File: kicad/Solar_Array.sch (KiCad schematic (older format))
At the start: 26 parts

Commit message: Changed XSHUT to pin header.
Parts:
- removed C?: C, symbol C
- removed C?: .1u, symbol C
- removed D?: ZENER, symbol ZENER
- removed R?: R, symbol R
- removed R?: 10k, symbol R
- removed SW?: SW_PUSH, symbol SW_PUSH
- added P?: X_SHUT, symbol CONN_01X01
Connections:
- wire segments 74 -> 66
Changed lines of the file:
@@
 	1    0    0    -1
-$EndComp
-$Comp
-L R R?
-U 1 1 56A86498
-P 16050 6750
-F 0 "R?" V 16130 6750 50  0000 C CNN
-F 1 "R" V 16050 6750 50  0000 C CNN
-F 2 "" V 15980 6750 30  0000 C CNN
-F 3 "" H 16050 6750 30  0000 C CNN
-	1    16050 6750
-	1    0    0    -1
-$EndComp
-$Comp
-L C C?
-U 1 1 56A86782
-P 16050 7300
-F 0 "C?" H 16075 7400 50  0000 L CNN
-F 1 "C" H 16075 7200 50  0000 L CNN
-F 2 "" H 16088 7150 30  0000 C CNN
-F 3 "" H 16050 7300 60  0000 C CNN
-	1    16050 7300
-	1    0    0    -1
-$EndComp
-$Comp
-L ZENER D?
-U 1 1 56A86C34
-P 16050 8000
-F 0 "D?" H 16050 8100 50  0000 C CNN
-F 1 "ZENER" H 16050 7900 50  0000 C CNN
-F 2 "" H 16050 8000 60  0000 C CNN
-F 3 "" H 16050 8000 60  0000 C CNN
-	1    16050 8000
-	0    1    1    0
 $EndComp
 Text Notes 1200 9750 0    60   ~ 0
@@
 	6050 1300 9000 1300
 Wire Wire Line
-	16050 5850 16050 6600
-Connection ~ 16050 5850
-Wire Wire Line
-	16050 6900 16050 7150
-Wire Wire Line
-	16050 7450 16050 7800
-Wire Wire Line
-	16050 8200 16050 8900
-Connection ~ 16050 8900
-Wire Wire Line
 	1400 2850 1550 2850
 Wire Wire Line
@@
 Connection ~ 3900 2250
 Wire Wire Line
-	3600 1700 5150 1700
-Wire Wire Line
 	3900 1350 3900 1800
 Connection ~ 4900 1700
@@
 	-1   0    0    1
 $EndComp
-$Comp
-L SW_PUSH SW?
-U 1 1 56A9E4AC
-P 3100 3650
-F 0 "SW?" H 3250 3760 50  0000 C CNN
-F 1 "SW_PUSH" H 3100 3570 50  0000 C CNN
-F 2 "" H 3100 3650 60  0000 C CNN
-F 3 "" H 3100 3650 60  0000 C CNN
-	1    3100 3650
-	0    1    1    0
-$EndComp
-Wire Wire Line
-	3100 3950 3100 4050
-$Comp
-L GND #PWR?
-U 1 1 56A9E5E0
-P 3100 4400
-F 0 "#PWR?" H 3100 4150 50  0001 C CNN
-F 1 "GND" H 3100 4250 50  0000 C CNN
-F 2 "" H 3100 4400 60  0000 C CNN
-F 3 "" H 3100 4400 60  0000 C CNN
-	1    3100 4400
-	1    0    0    -1
-$EndComp
-Wire Wire Line
-	3100 1700 3100 3350
 Wire Wire Line
 	3100 3300 3250 3300
-Wire Wire Line
-	3100 1700 3300 1700
 Connection ~ 3100 3300
-$Comp
-L C C?
-U 1 1 56A9E786
-P 3450 1700
-F 0 "C?" H 3475 1800 50  0000 L CNN
-F 1 ".1u" H 3475 1600 50  0000 L CNN
-F 2 "" H 3488 1550 30  0000 C CNN
-F 3 "" H 3450 1700 60  0000 C CNN
-	1    3450 1700
-	0    1    1    0
-$EndComp
-$Comp
-L R R?
-U 1 1 56A9EACC
-P 3100 4200
-F 0 "R?" V 3180 4200 50  0000 C CNN
-F 1 "10k" V 3100 4200 50  0000 C CNN
-F 2 "" V 3030 4200 30  0000 C CNN
-F 3 "" H 3100 4200 30  0000 C CNN
-	1    3100 4200
-	1    0    0    -1
-$EndComp
-Wire Wire Line
-	3100 4350 3100 4400
+Wire Wire Line
+	3900 1700 5150 1700
+$Comp
+L CONN_01X01 P?
+U 1 1 56AA3494
+P 2900 3300
+F 0 "P?" H 2900 3400 50  0000 C CNN
+F 1 "X_SHUT" H 2900 3200 50  0000 C CNN
+F 2 "" H 2900 3300 60  0000 C CNN
+F 3 "" H 2900 3300 60  0000 C CNN
+	1    2900 3300
+	-1   0    0    1
+$EndComp
 $EndSCHEMATC

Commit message: Removed extraneous circuitry, added more component values, swapped 1x2 conn with 1x3 conn.
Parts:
- removed C?: .1u, symbol C
- removed P?: V_BATT, symbol CONN_01X02
- added D?: D_Schottky, symbol D_Schottky
- added P?: V_BATT, symbol CONN_01X03
- R?: value R -> .007
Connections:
- net labels removed: +5V
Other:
- note added: "VCC_IN"
- moved on the sheet: P?
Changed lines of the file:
@@
-	1    0    0    -1
-$EndComp
-$Comp
-L +5V #PWR?
-U 1 1 56A796A0
-P 7300 1800
-F 0 "#PWR?" H 7300 1650 50  0001 C CNN
-F 1 "+5V" H 7300 1940 50  0000 C CNN
-F 2 "" H 7300 1800 60  0000 C CNN
-F 3 "" H 7300 1800 60  0000 C CNN
-	1    7300 1800
 	1    0    0    -1
 $EndComp
@@
 L GND #PWR?
 U 1 1 56A96BD7
-P 1550 2950
-F 0 "#PWR?" H 1550 2700 50  0001 C CNN
-F 1 "GND" H 1550 2800 50  0000 C CNN
-F 2 "" H 1550 2950 60  0000 C CNN
-F 3 "" H 1550 2950 60  0000 C CNN
-	1    1550 2950
+P 1250 3100
+F 0 "#PWR?" H 1250 2850 50  0001 C CNN
+F 1 "GND" H 1250 2950 50  0000 C CNN
+F 2 "" H 1250 3100 60  0000 C CNN
+F 3 "" H 1250 3100 60  0000 C CNN
+	1    1250 3100
 	1    0    0    -1
 $EndComp
@@
 P 4900 2250
 F 0 "R?" V 4980 2250 50  0000 C CNN
-F 1 "R" V 4900 2250 50  0000 C CNN
+F 1 ".007" V 4900 2250 50  0000 C CNN
 F 2 "" V 4830 2250 30  0000 C CNN
 F 3 "" H 4900 2250 30  0000 C CNN
@@
 	7000 3350 7000 3600
 Wire Wire Line
-	7300 1800 7300 2150
+	7300 1050 7300 2150
 Wire Wire Line
 	7600 2950 7850 2950
@@
 Wire Notes Line
 	6050 1300 9000 1300
-Wire Wire Line
-	1400 2850 1550 2850
-Wire Wire Line
-	1550 2850 1550 2950
-Wire Wire Line
-	1400 2750 2450 2750
 Wire Wire Line
 	2350 2750 2350 3050
@@
 Wire Wire Line
 	4700 2250 4550 2250
-$Comp
-L GND #PWR?
-U 1 1 56A9D3E6
-P 2500 2350
-F 0 "#PWR?" H 2500 2100 50  0001 C CNN
-F 1 "GND" H 2500 2200 50  0000 C CNN
-F 2 "" H 2500 2350 60  0000 C CNN
-F 3 "" H 2500 2350 60  0000 C CNN
-	1    2500 2350
-	1    0    0    -1
-$EndComp
-$Comp
-L C C?
-U 1 1 56A9D482
-P 2850 2250
-F 0 "C?" H 2875 2350 50  0000 L CNN
-F 1 ".1u" H 2875 2150 50  0000 L CNN
-F 2 "" H 2888 2100 30  0000 C CNN
-F 3 "" H 2850 2250 60  0000 C CNN
-	1    2850 2250
-	0    1    1    0
-$EndComp
-Wire Wire Line
-	2700 2250 2500 2250
-Wire Wire Line
-	2500 2250 2500 2350
-Wire Wire Line
-	3000 2250 4250 2250
 Connection ~ 3900 2250
 Wire Wire Line
@@
 Wire Wire Line
 	6000 1150 4000 1150
-$Comp
-L CONN_01X02 P?
-U 1 1 56A9DC7C
-P 9450 1000
-F 0 "P?" H 9450 1150 50  0000 C CNN
-F 1 "V_BATT" V 9550 1000 50  0000 C CNN
-F 2 "" H 9450 1000 60  0000 C CNN
-F 3 "" H 9450 1000 60  0000 C CNN
-	1    9450 1000
-	1    0    0    -1
-$EndComp
 Wire Wire Line
 	3900 950  9250 950
-Wire Wire Line
-	9250 1050 9150 1050
-Wire Wire Line
-	9150 1050 9150 1300
 $Comp
 L GND #PWR?
@@
 L CONN_01X02 P?
 U 1 1 56A9E16B
-P 1200 2800
-F 0 "P?" H 1200 2950 50  0000 C CNN
-F 1 "PV_CELL" V 1300 2800 50  0000 C CNN
-F 2 "" H 1200 2800 60  0000 C CNN
-F 3 "" H 1200 2800 60  0000 C CNN
-	1    1200 2800
+P 850 2800
+F 0 "P?" H 850 2950 50  0000 C CNN
+F 1 "PV_CELL" V 950 2800 50  0000 C CNN
+F 2 "" H 850 2800 60  0000 C CNN
+F 3 "" H 850 2800 60  0000 C CNN
+	1    850  2800
 	-1   0    0    1
 $EndComp
@@
 	-1   0    0    1
 $EndComp
+Wire Wire Line
+	3900 2250 4250 2250
+$Comp
+L CONN_01X03 P?
+U 1 1 56AA5ABE
+P 9450 1050
+F 0 "P?" H 9450 1250 50  0000 C CNN
+F 1 "V_BATT" H 9650 1150 50  0000 C CNN
+F 2 "" H 9450 1050 60  0000 C CNN
+F 3 "" H 9450 1050 60  0000 C CNN
+	1    9450 1050
+	1    0    0    -1
+$EndComp
+Wire Wire Line
+	9150 1150 9250 1150
+Wire Wire Line
+	9150 1150 9150 1300
+Wire Wire Line
+	7300 1050 9250 1050
+Text Notes 9550 1050 0    50   ~ 0
+VCC_IN
+$Comp
+L D_Schottky D?
+U 1 1 56AA70D2
+P 1500 2750
+F 0 "D?" H 1500 2850 50  0000 C CNN
+F 1 "D_Schottky" H 1500 2650 50  0000 C CNN
+F 2 "" H 1500 2750 60  0000 C CNN
+F 3 "" H 1500 2750 60  0000 C CNN
+	1    1500 2750
+	-1   0    0    1
+$EndComp
+Wire Wire Line
+	1050 2750 1350 2750
+Wire Wire Line
+	1050 2850 1250 2850
+Wire Wire Line
+	1250 2850 1250 3100
+Wire Wire Line
+	1650 2750 2450 2750
 $EndSCHEMATC

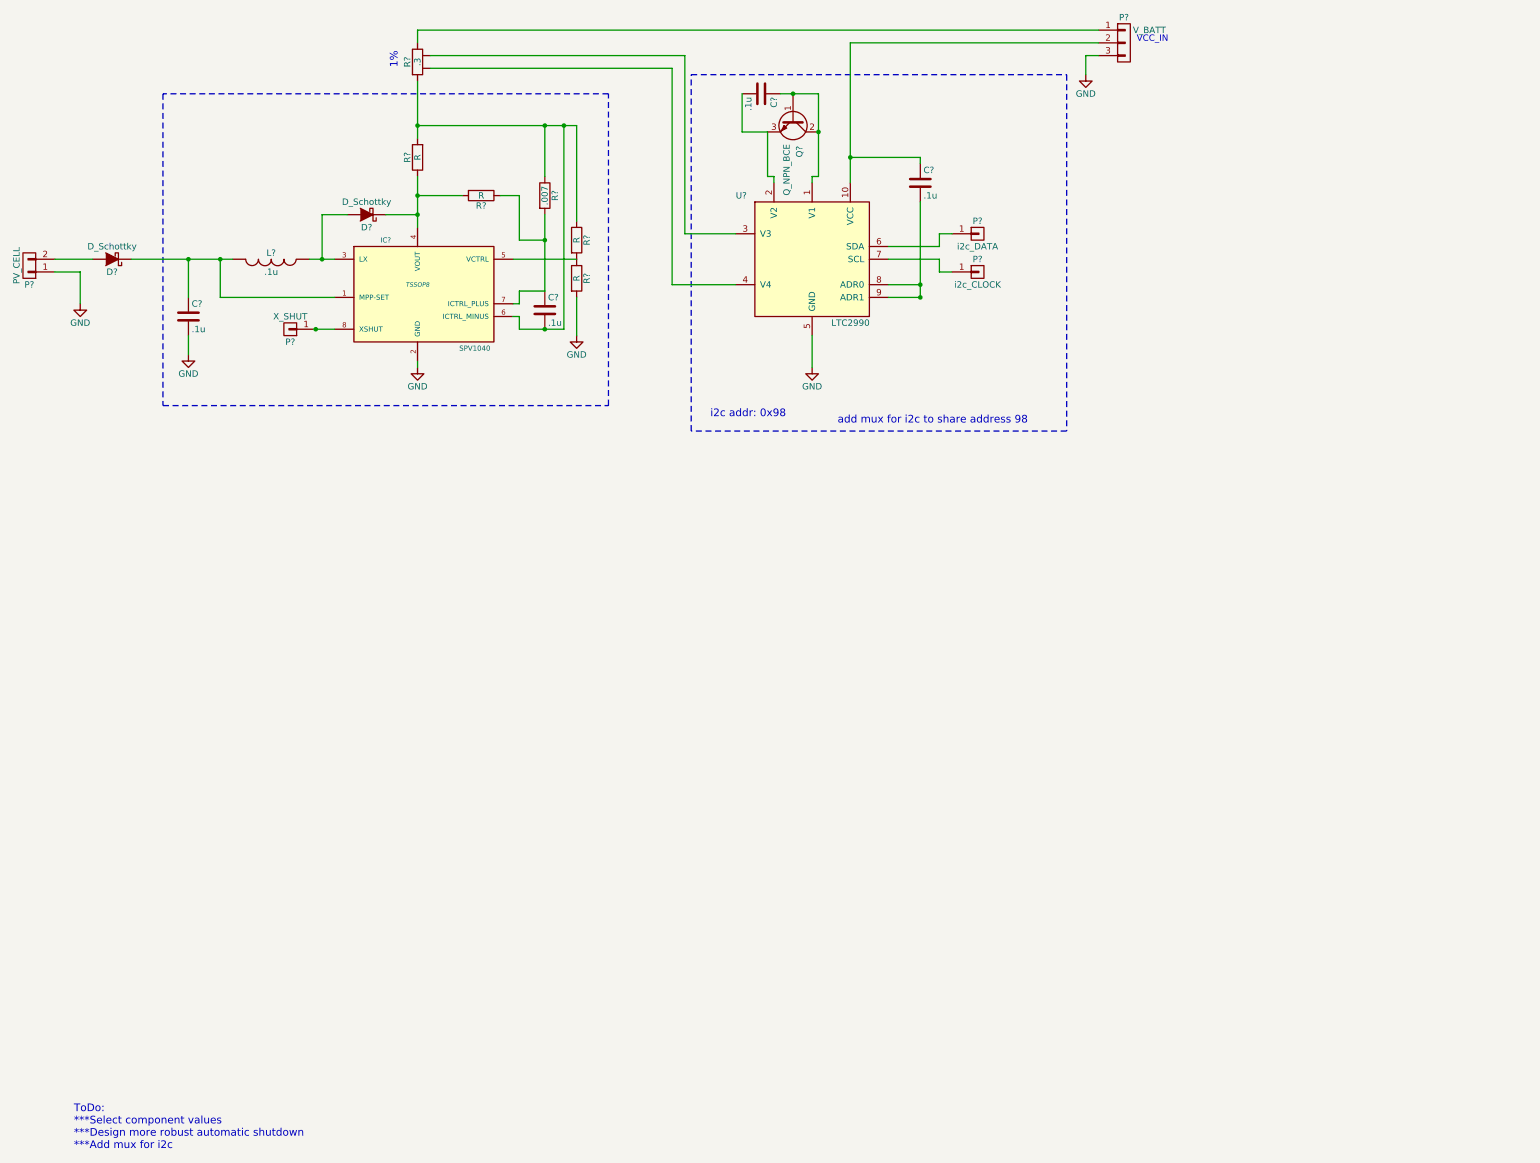
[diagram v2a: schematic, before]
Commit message: Changed Requirements, Notes, Outputs. Added Reference Switch.  Design Docs Updated.
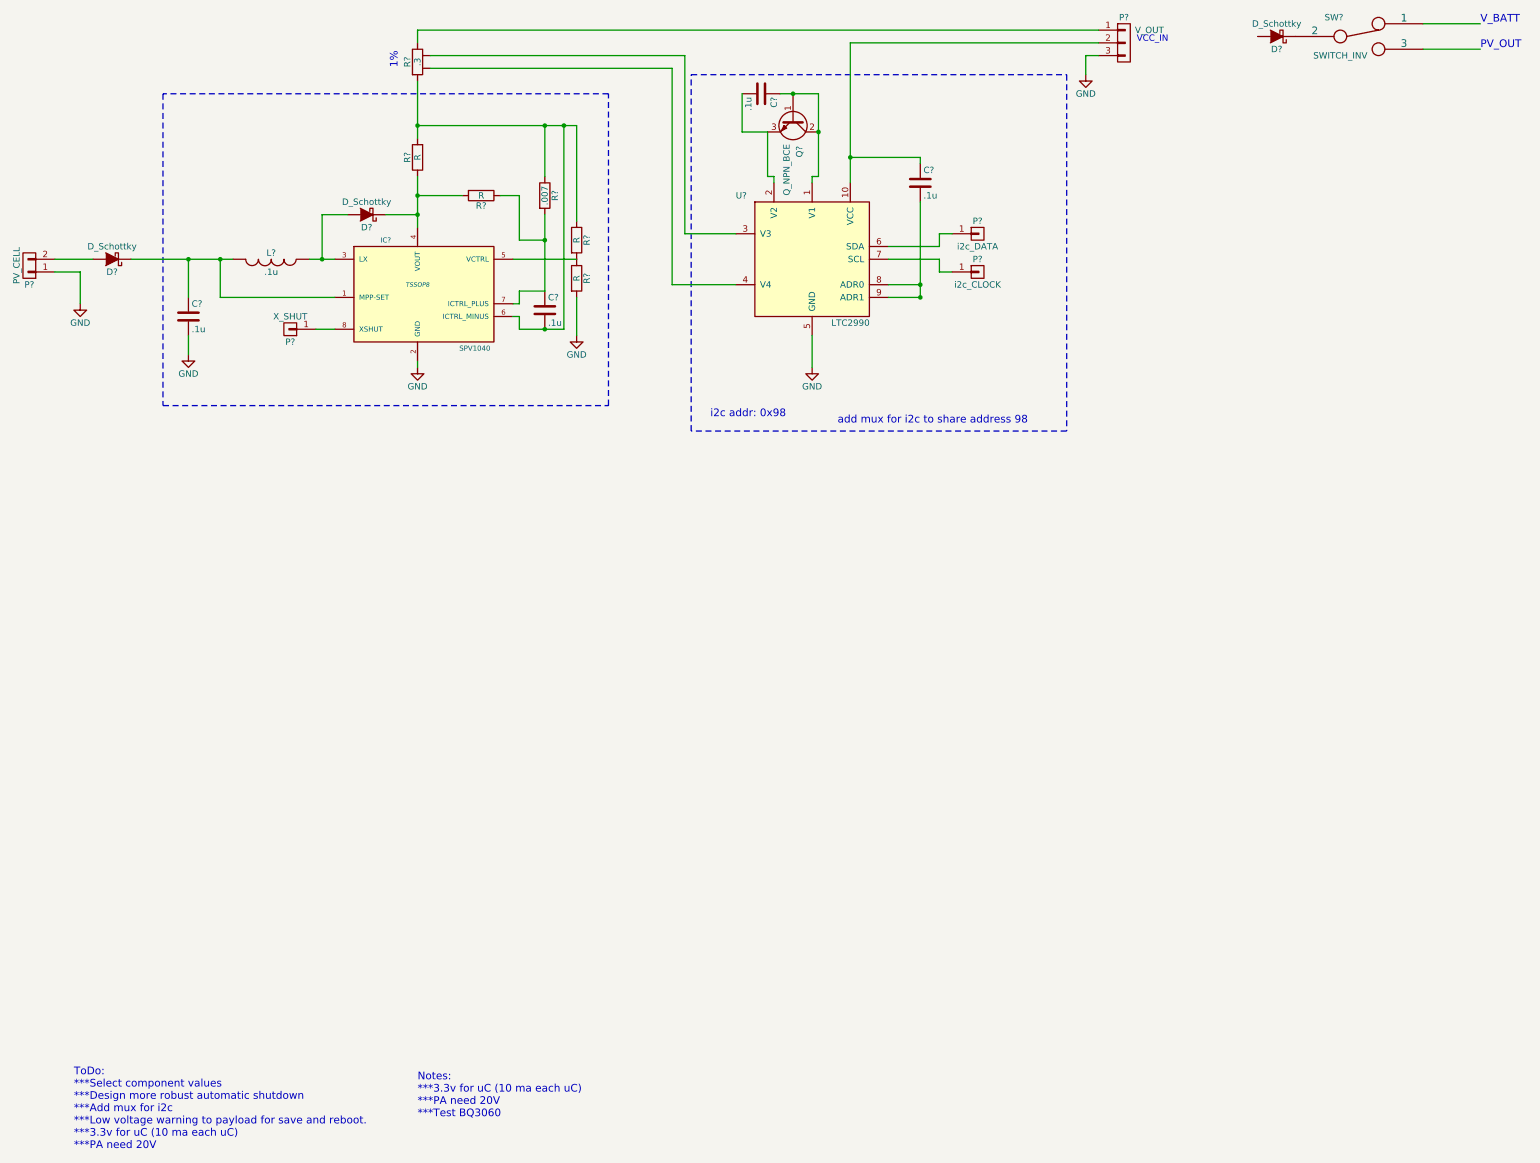
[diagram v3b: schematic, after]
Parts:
- added D?: D_Schottky, symbol D_Schottky
- added SW?: SWITCH_INV, symbol SWITCH_INV
- P?: value V_BATT -> V_OUT
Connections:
- new net: D?.1 (K), SW?.2
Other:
- note added: "Notes:\n***3.3v for uC (10 ma each uC)\n***PA need 20V\n***Test BQ3060"
- note added: "PV_OUT"
- note added: "ToDo:\n***Select component values\n***Design more robust automatic shutdown\n***Add mux for i2c\n***Low voltage warning to payload for save and reboot.\n***3.3v for uC (10 ma each uC)\n***PA need 20V"
- note added: "V_BATT"
- note removed: "ToDo:\n***Select component values\n***Design more robust automatic shutdown\n***Add mux for i2c\n"
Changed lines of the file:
@@
 $EndComp
 Text Notes 1200 9750 0    60   ~ 0
-ToDo:\n***Select component values\n***Design more robust automatic shutdown\n***Add mux for i2c\n
+ToDo:\n***Select component values\n***Design more robust automatic shutdown\n***Add mux for i2c\n***Low voltage warning to payload for save and reboot.\n***3.3v for uC (10 ma each uC)\n***PA need 20V
 Text Notes 3750 1250 1    60   ~ 0
 1%
@@
 	1    0    0    -1
 $EndComp
-Wire Wire Line
-	7000 3350 7000 3600
-Wire Wire Line
-	7300 1050 7300 2150
-Wire Wire Line
-	7600 2950 7850 2950
-Wire Wire Line
-	7850 3050 7600 3050
-Connection ~ 7850 3050
-Connection ~ 7850 2950
-Wire Wire Line
-	7850 2000 7850 1950
-Wire Wire Line
-	7850 1950 7300 1950
-Connection ~ 7300 1950
-Wire Notes Line
-	9000 1300 9000 4100
-Wire Notes Line
-	9000 4100 6050 4100
-Wire Notes Line
-	6050 4100 6050 1300
-Wire Wire Line
-	7850 2300 7850 3050
-Wire Wire Line
-	5900 2950 6400 2950
-Wire Wire Line
-	6000 2550 6400 2550
-Wire Wire Line
-	7000 2150 7000 2100
-Wire Wire Line
-	7000 2100 7050 2100
-Wire Wire Line
-	7050 2100 7050 1450
-Wire Wire Line
-	6700 2150 6700 2100
-Wire Wire Line
-	6700 2100 6650 2100
-Wire Wire Line
-	6650 2100 6650 1750
-Wire Wire Line
-	6650 1750 6450 1750
-Wire Wire Line
-	6450 1750 6450 1450
-Wire Wire Line
-	7050 1450 6750 1450
-Connection ~ 7050 1750
-Connection ~ 6850 1450
-Wire Notes Line
-	6050 1300 9000 1300
-Wire Wire Line
-	2350 2750 2350 3050
-Wire Wire Line
-	2350 3050 3250 3050
-Wire Wire Line
-	2100 2750 2100 3050
-Connection ~ 2350 2750
-Wire Wire Line
-	2100 3350 2100 3500
-Wire Wire Line
-	3050 2750 3250 2750
-Wire Wire Line
-	4650 3200 4700 3200
-Wire Wire Line
-	4700 3200 4700 3300
-Wire Wire Line
-	4700 3300 5050 3300
-Wire Wire Line
-	4700 3100 4650 3100
-Wire Wire Line
-	4650 2750 5150 2750
-Wire Wire Line
-	5150 3050 5150 3350
-Wire Wire Line
-	3150 2750 3150 2400
-Connection ~ 3150 2750
-Wire Wire Line
-	3150 2400 3350 2400
-Connection ~ 3900 2400
-Wire Wire Line
-	5150 1700 5150 2450
-Wire Wire Line
-	4900 1700 4900 2100
-Wire Wire Line
-	3900 2100 3900 2500
-Wire Wire Line
-	3900 3550 3900 3600
-Wire Notes Line
-	5400 3900 5400 1450
-Wire Notes Line
-	5400 1450 1900 1450
-Wire Notes Line
-	1900 1450 1900 3900
-Wire Notes Line
-	1900 3900 5400 3900
-Wire Wire Line
-	5900 1250 5900 2950
-Wire Wire Line
-	6000 1150 6000 2550
-Connection ~ 2100 2750
 $Comp
 L CONN_01X01 P?
@@
 	1    0    0    -1
 $EndComp
-Wire Wire Line
-	7600 2750 8000 2750
-Wire Wire Line
-	8000 2750 8000 2850
-Wire Wire Line
-	8000 2850 8100 2850
 $Comp
 L CONN_01X01 P?
@@
 	1    0    0    -1
 $EndComp
-Wire Wire Line
-	7600 2650 8000 2650
-Wire Wire Line
-	8000 2650 8000 2550
-Wire Wire Line
-	8000 2550 8100 2550
-Wire Wire Line
-	4700 2250 4700 2600
-Wire Wire Line
-	4700 2600 4900 2600
-Wire Wire Line
-	4900 2400 4900 3000
-Connection ~ 4900 2600
-Wire Wire Line
-	4700 3100 4700 3000
-Wire Wire Line
-	4700 3000 4900 3000
-Wire Wire Line
-	5050 3300 5050 1700
-Connection ~ 4900 3300
-Wire Wire Line
-	3650 2400 3900 2400
-Wire Wire Line
-	4700 2250 4550 2250
-Connection ~ 3900 2250
-Wire Wire Line
-	3900 1350 3900 1800
-Connection ~ 4900 1700
-Connection ~ 5050 1700
-Connection ~ 3900 1700
-Wire Wire Line
-	5900 1250 4000 1250
-Wire Wire Line
-	6000 1150 4000 1150
-Wire Wire Line
-	3900 950  9250 950
 $Comp
 L GND #PWR?
@@
 	1    0    0    -1
 $EndComp
-Wire Wire Line
-	3900 950  3900 1050
 $Comp
 L CONN_01X02 P?
@@
 	-1   0    0    1
 $EndComp
-Wire Wire Line
-	3100 3300 3250 3300
-Connection ~ 3100 3300
-Wire Wire Line
-	3900 1700 5150 1700
 $Comp
 L CONN_01X01 P?
@@
 	-1   0    0    1
 $EndComp
-Wire Wire Line
-	3900 2250 4250 2250
 $Comp
 L CONN_01X03 P?
@@
 P 9450 1050
 F 0 "P?" H 9450 1250 50  0000 C CNN
-F 1 "V_BATT" H 9650 1150 50  0000 C CNN
+F 1 "V_OUT" H 9650 1150 50  0000 C CNN
 F 2 "" H 9450 1050 60  0000 C CNN
 F 3 "" H 9450 1050 60  0000 C CNN
@@
 	1    0    0    -1
 $EndComp
-Wire Wire Line
-	9150 1150 9250 1150
-Wire Wire Line
-	9150 1150 9150 1300
-Wire Wire Line
-	7300 1050 9250 1050
 Text Notes 9550 1050 0    50   ~ 0
 VCC_IN
@@
 	-1   0    0    1
 $EndComp
+Text Notes 3900 9500 0    60   ~ 0
+Notes:\n***3.3v for uC (10 ma each uC)\n***PA need 20V\n***Test BQ3060
+Wire Wire Line
+	7000 3350 7000 3600
+Wire Wire Line
+	7300 1050 7300 2150
+Wire Wire Line
+	7600 2950 7850 2950
+Wire Wire Line
+	7850 3050 7600 3050
+Connection ~ 7850 3050
+Connection ~ 7850 2950
+Wire Wire Line
+	7850 2000 7850 1950
+Wire Wire Line
+	7850 1950 7300 1950
+Connection ~ 7300 1950
+Wire Notes Line
+	9000 1300 9000 4100
+Wire Notes Line
+	9000 4100 6050 4100
+Wire Notes Line
+	6050 4100 6050 1300
+Wire Wire Line
+	7850 2300 7850 3050
+Wire Wire Line
+	5900 2950 6400 2950
+Wire Wire Line
+	6000 2550 6400 2550
+Wire Wire Line
+	7000 2150 7000 2100
+Wire Wire Line
+	7000 2100 7050 2100
+Wire Wire Line
+	7050 2100 7050 1450
+Wire Wire Line
+	6700 2150 6700 2100
+Wire Wire Line
+	6700 2100 6650 2100
+Wire Wire Line
+	6650 2100 6650 1750
+Wire Wire Line
+	6650 1750 6450 1750
+Wire Wire Line
+	6450 1750 6450 1450
+Wire Wire Line
+	7050 1450 6750 1450
+Connection ~ 7050 1750
+Connection ~ 6850 1450
+Wire Notes Line
+	6050 1300 9000 1300
+Wire Wire Line
+	2350 2750 2350 3050
+Wire Wire Line
+	2350 3050 3250 3050
+Wire Wire Line
+	2100 2750 2100 3050
+Connection ~ 2350 2750
+Wire Wire Line
+	2100 3350 2100 3500
+Wire Wire Line
+	3050 2750 3250 2750
+Wire Wire Line
+	4650 3200 4700 3200
+Wire Wire Line
+	4700 3200 4700 3300
+Wire Wire Line
+	4700 3300 5050 3300
+Wire Wire Line
+	4700 3100 4650 3100
+Wire Wire Line
+	4650 2750 5150 2750
+Wire Wire Line
+	5150 3050 5150 3350
+Wire Wire Line
+	3150 2750 3150 2400
+Connection ~ 3150 2750
+Wire Wire Line
+	3150 2400 3350 2400
+Connection ~ 3900 2400
+Wire Wire Line
+	5150 1700 5150 2450
+Wire Wire Line
+	4900 1700 4900 2100
+Wire Wire Line
+	3900 2100 3900 2500
+Wire Wire Line
+	3900 3550 3900 3600
+Wire Notes Line
+	5400 3900 5400 1450
+Wire Notes Line
+	5400 1450 1900 1450
+Wire Notes Line
+	1900 1450 1900 3900
+Wire Notes Line
+	1900 3900 5400 3900
+Wire Wire Line
+	5900 1250 5900 2950
+Wire Wire Line
+	6000 1150 6000 2550
+Connection ~ 2100 2750
+Wire Wire Line
+	7600 2750 8000 2750
+Wire Wire Line
+	8000 2750 8000 2850
+Wire Wire Line
+	8000 2850 8100 2850
+Wire Wire Line
+	7600 2650 8000 2650
+Wire Wire Line
+	8000 2650 8000 2550
+Wire Wire Line
+	8000 2550 8100 2550
+Wire Wire Line
+	4700 2250 4700 2600
+Wire Wire Line
+	4700 2600 4900 2600
+Wire Wire Line
+	4900 2400 4900 3000
+Connection ~ 4900 2600
+Wire Wire Line
+	4700 3100 4700 3000
+Wire Wire Line
+	4700 3000 4900 3000
+Wire Wire Line
+	5050 3300 5050 1700
+Connection ~ 4900 3300
+Wire Wire Line
+	3650 2400 3900 2400
+Wire Wire Line
+	4700 2250 4550 2250
+Connection ~ 3900 2250
+Wire Wire Line
+	3900 1350 3900 1800
+Connection ~ 4900 1700
+Connection ~ 5050 1700
+Connection ~ 3900 1700
+Wire Wire Line
+	5900 1250 4000 1250
+Wire Wire Line
+	6000 1150 4000 1150
+Wire Wire Line
+	3900 950  9250 950
+Wire Wire Line
+	3900 950  3900 1050
+Wire Wire Line
+	3100 3300 3250 3300
+Wire Wire Line
+	3900 1700 5150 1700
+Wire Wire Line
+	3900 2250 4250 2250
+Wire Wire Line
+	9150 1150 9250 1150
+Wire Wire Line
+	9150 1150 9150 1300
+Wire Wire Line
+	7300 1050 9250 1050
 Wire Wire Line
 	1050 2750 1350 2750
@@
 Wire Wire Line
 	1650 2750 2450 2750
+$Comp
+L D_Schottky D?
+U 1 1 56AC3033
+P 10650 1000
+F 0 "D?" H 10650 1100 50  0000 C CNN
+F 1 "D_Schottky" H 10650 900 50  0000 C CNN
+F 2 "" H 10650 1000 60  0000 C CNN
+F 3 "" H 10650 1000 60  0000 C CNN
+	1    10650 1000
+	-1   0    0    1
+$EndComp
+$Comp
+L SWITCH_INV SW?
+U 1 1 56AC30B8
+P 11300 1000
+F 0 "SW?" H 11100 1150 50  0000 C CNN
+F 1 "SWITCH_INV" H 11150 850 50  0000 C CNN
+F 2 "" H 11300 1000 60  0000 C CNN
+F 3 "" H 11300 1000 60  0000 C CNN
+	1    11300 1000
+	1    0    0    -1
+$EndComp
+Wire Wire Line
+	11800 900  12250 900
+Wire Wire Line
+	11800 1100 12250 1100
+Text Notes 12250 900  0    60   ~ 0
+V_BATT
+Text Notes 12250 1100 0    60   ~ 0
+PV_OUT
 $EndSCHEMATC
